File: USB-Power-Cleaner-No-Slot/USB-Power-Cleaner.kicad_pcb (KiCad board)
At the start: 2 copper layers, 43.7 x 17.8 mm, 7 parts, among them J1 USB3_A, J2 USB3_A

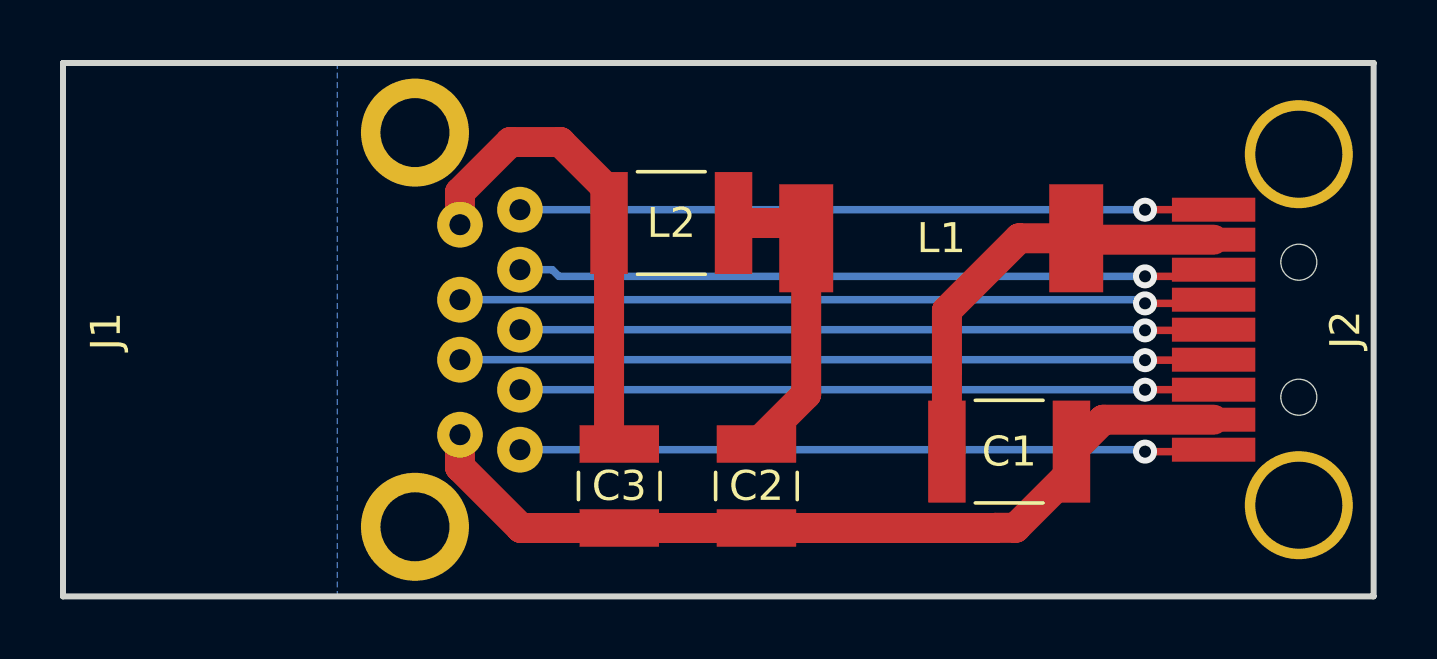
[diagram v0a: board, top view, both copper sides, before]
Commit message: Changed stuff to work better on oshpark board constraints
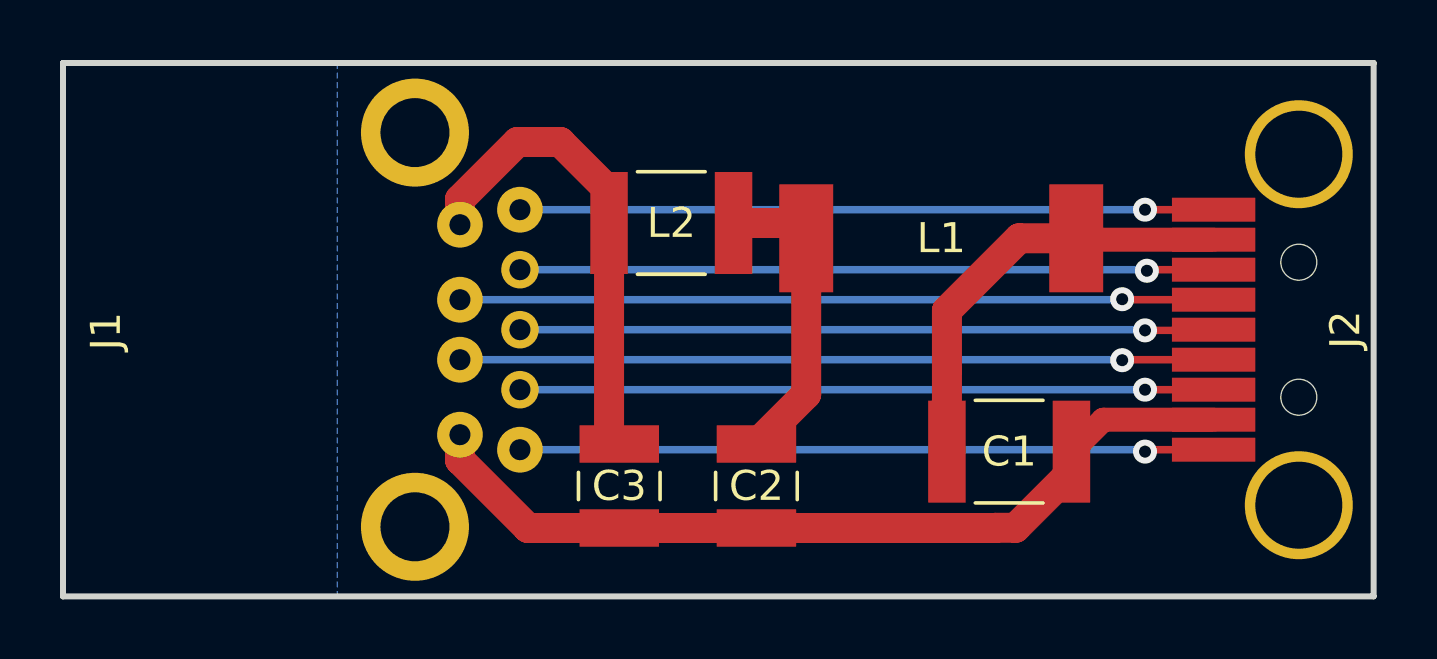
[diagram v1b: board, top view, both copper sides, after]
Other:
- net class Default: clearance 0.1 -> 0.2
- net class Power: clearance 0.1 -> 0.2
- rule trace_clearance: 0.1 -> 0.2
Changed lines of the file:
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@@
     (thickness 1.6)
     (drawings 5)
-    (tracks 62)
+    (tracks 61)
     (zones 0)
     (modules 7)
@@
   (setup
     (last_trace_width 0.25)
-    (trace_clearance 0.1)
+    (trace_clearance 0.2)
     (zone_clearance 0.25)
     (zone_45_only no)
@@
     (mod_text_size 1 1)
     (mod_text_width 0.15)
-    (pad_size 1.524 1.524)
-    (pad_drill 0.762)
+    (pad_size 1.25 1.25)
+    (pad_drill 0.7)
     (pad_to_mask_clearance 0.1)
     (aux_axis_origin 0 0)
@@
   (net 12 "Net-(J1-Pad10)")
   (net_class Default "This is the default net class."
-    (clearance 0.1)
+    (clearance 0.2)
     (trace_width 0.25)
     (via_dia 0.8)
@@
   )
   (net_class Power ""
-    (clearance 0.1)
+    (clearance 0.2)
     (trace_width 1)
     (via_dia 0.8)
@@
     (fp_line (start -7.95 8.35) (end 7.95 8.35) (layer F.CrtYd) (width 0.05))
     (fp_line (start -7.95 8.35) (end -7.95 -8.35) (layer F.CrtYd) (width 0.05))
-    (pad 7 thru_hole circle (at 0 -6.85 270) (size 1.524 1.524) (drill 0.7) (layers *.Cu *.Mask)
+    (pad 7 thru_hole circle (at 0 -6.85 270) (size 1.25 1.25) (drill 0.7) (layers *.Cu *.Mask)
       (net 5 "Net-(J1-Pad7)"))
-    (pad 8 thru_hole circle (at -2 -6.85 270) (size 1.524 1.524) (drill 0.7) (layers *.Cu *.Mask)
+    (pad 8 thru_hole circle (at -2 -6.85 270) (size 1.25 1.25) (drill 0.7) (layers *.Cu *.Mask)
       (net 6 "Net-(J1-Pad8)"))
     (pad 9 thru_hole circle (at -4 -6.85 270) (size 1.524 1.524) (drill 0.7) (layers *.Cu *.Mask)
       (net 7 "Net-(J1-Pad9)"))
-    (pad 6 thru_hole circle (at 2 -6.85 270) (size 1.524 1.524) (drill 0.7) (layers *.Cu *.Mask)
+    (pad 6 thru_hole circle (at 2 -6.85 270) (size 1.25 1.25) (drill 0.7) (layers *.Cu *.Mask)
       (net 8 "Net-(J1-Pad6)"))
     (pad 5 thru_hole circle (at 4 -6.85 270) (size 1.524 1.524) (drill 0.7) (layers *.Cu *.Mask)
@@
   (gr_line (start 157.226 78.74) (end 200.914 78.74) (layer Edge.Cuts) (width 0.2))
   (segment (start 186.69 91.635) (end 186.69 92.71) (width 1) (layer F.Cu) (net 1))
-  (segment (start 191.048 84.63) (end 195.58 84.63) (width 1) (layer F.Cu) (net 1))
+  (segment (start 191.048 84.63) (end 195.58 84.63) (width 0.8) (layer F.Cu) (net 1))
   (segment (start 191 84.582) (end 191.048 84.63) (width 1) (layer F.Cu) (net 1))
   (segment (start 186.69 88.994) (end 186.69 91.694) (width 1) (layer F.Cu) (net 1))
@@
   (segment (start 189.1 84.582) (end 186.69 86.992) (width 1) (layer F.Cu) (net 1))
   (segment (start 191 84.582) (end 189.1 84.582) (width 1) (layer F.Cu) (net 1))
-  (segment (start 173.443 94.24) (end 175.768 94.24) (width 1) (layer F.Cu) (net 2))
-  (segment (start 172.49037 94.24) (end 173.443 94.24) (width 1) (layer F.Cu) (net 2))
-  (segment (start 170.458 92.20763) (end 172.49037 94.24) (width 1) (layer F.Cu) (net 2))
-  (segment (start 170.458 91.13) (end 170.458 92.20763) (width 1) (layer F.Cu) (net 2))
   (segment (start 175.768 94.24) (end 180.34 94.24) (width 1) (layer F.Cu) (net 2))
-  (segment (start 191.904 90.63) (end 190.84 91.694) (width 1) (layer F.Cu) (net 2))
-  (segment (start 195.58 90.63) (end 191.904 90.63) (width 1) (layer F.Cu) (net 2))
+  (segment (start 191.904 90.63) (end 190.84 91.694) (width 0.8) (layer F.Cu) (net 2))
+  (segment (start 195.58 90.63) (end 191.904 90.63) (width 0.8) (layer F.Cu) (net 2))
   (segment (start 190.84 92.37) (end 190.84 91.694) (width 1) (layer F.Cu) (net 2))
   (segment (start 188.976 94.234) (end 190.84 92.37) (width 1) (layer F.Cu) (net 2))
@@
   (segment (start 188.294 94.24) (end 188.3 94.234) (width 1) (layer F.Cu) (net 2))
   (segment (start 180.34 94.24) (end 188.294 94.24) (width 1) (layer F.Cu) (net 2))
+  (segment (start 173.443 94.24) (end 175.768 94.24) (width 1) (layer F.Cu) (net 2))
+  (segment (start 172.726 94.24) (end 173.443 94.24) (width 1) (layer F.Cu) (net 2))
+  (segment (start 170.458 91.972) (end 172.726 94.24) (width 1) (layer F.Cu) (net 2))
+  (segment (start 170.458 91.13) (end 170.458 91.972) (width 1) (layer F.Cu) (net 2))
   (segment (start 181.492 84.074) (end 182 84.582) (width 1) (layer F.Cu) (net 3))
   (segment (start 179.578 84.074) (end 181.492 84.074) (width 1) (layer F.Cu) (net 3))
   (segment (start 182 89.78) (end 180.34 91.44) (width 1) (layer F.Cu) (net 3))
   (segment (start 182 84.582) (end 182 89.78) (width 1) (layer F.Cu) (net 3))
-  (segment (start 175.428 82.999) (end 175.428 84.074) (width 1) (layer F.Cu) (net 4))
-  (segment (start 173.803 81.374) (end 175.428 82.999) (width 1) (layer F.Cu) (net 4))
-  (segment (start 172.13637 81.374) (end 173.803 81.374) (width 1) (layer F.Cu) (net 4))
-  (segment (start 170.458 83.05237) (end 172.13637 81.374) (width 1) (layer F.Cu) (net 4))
-  (segment (start 170.458 84.13) (end 170.458 83.05237) (width 1) (layer F.Cu) (net 4))
   (segment (start 175.428 91.1) (end 175.768 91.44) (width 1) (layer F.Cu) (net 4))
   (segment (start 175.428 84.074) (end 175.428 91.1) (width 1) (layer F.Cu) (net 4))
+  (segment (start 175.428 82.999) (end 175.428 84.074) (width 1) (layer F.Cu) (net 4))
+  (segment (start 170.458 83.288) (end 172.372 81.374) (width 1) (layer F.Cu) (net 4))
+  (segment (start 173.803 81.374) (end 175.428 82.999) (width 1) (layer F.Cu) (net 4))
+  (segment (start 172.372 81.374) (end 173.803 81.374) (width 1) (layer F.Cu) (net 4))
+  (segment (start 170.458 84.13) (end 170.458 83.288) (width 1) (layer F.Cu) (net 4))
   (via (at 193.294 87.652006) (size 0.8) (drill 0.4) (layers F.Cu B.Cu) (net 5))
   (segment (start 193.271994 87.63) (end 193.294 87.652006) (width 0.25) (layer B.Cu) (net 5))
@@
   (segment (start 195.557994 87.652006) (end 195.58 87.63) (width 0.25) (layer F.Cu) (net 5))
   (segment (start 193.294 87.652006) (end 195.557994 87.652006) (width 0.25) (layer F.Cu) (net 5))
-  (segment (start 173.53563 85.63) (end 173.75763 85.852) (width 0.25) (layer B.Cu) (net 6))
-  (segment (start 172.458 85.63) (end 173.53563 85.63) (width 0.25) (layer B.Cu) (net 6))
-  (via (at 193.294 85.852) (size 0.8) (drill 0.4) (layers F.Cu B.Cu) (net 6))
-  (segment (start 173.75763 85.852) (end 193.294 85.852) (width 0.25) (layer B.Cu) (net 6))
-  (segment (start 195.358 85.852) (end 195.58 85.63) (width 0.25) (layer F.Cu) (net 6))
-  (segment (start 193.294 85.852) (end 195.358 85.852) (width 0.25) (layer F.Cu) (net 6))
+  (segment (start 172.458 85.63) (end 193.320926 85.63) (width 0.25) (layer B.Cu) (net 6))
+  (segment (start 195.58 85.63) (end 193.391536 85.63) (width 0.25) (layer F.Cu) (net 6))
+  (segment (start 193.391536 85.63) (end 193.356231 85.665305) (width 0.25) (layer F.Cu) (net 6))
+  (segment (start 193.320926 85.63) (end 193.356231 85.665305) (width 0.25) (layer B.Cu) (net 6))
+  (via (at 193.356231 85.665305) (size 0.8) (drill 0.4) (layers F.Cu B.Cu) (net 6))
   (via (at 193.294 83.63) (size 0.8) (drill 0.4) (layers F.Cu B.Cu) (net 7))
   (segment (start 172.458 83.63) (end 193.294 83.63) (width 0.25) (layer B.Cu) (net 7))
@@
   (segment (start 172.458 89.63) (end 193.294 89.63) (width 0.25) (layer B.Cu) (net 8))
   (segment (start 193.294 89.63) (end 195.58 89.63) (width 0.25) (layer F.Cu) (net 8))
-  (via (at 193.294 91.694) (size 0.8) (drill 0.4) (layers F.Cu B.Cu) (net 9))
-  (segment (start 193.23 91.63) (end 193.294 91.694) (width 0.25) (layer B.Cu) (net 9))
-  (segment (start 172.458 91.63) (end 193.23 91.63) (width 0.25) (layer B.Cu) (net 9))
-  (segment (start 195.516 91.694) (end 195.58 91.63) (width 0.25) (layer F.Cu) (net 9))
-  (segment (start 193.294 91.694) (end 195.516 91.694) (width 0.25) (layer F.Cu) (net 9))
-  (via (at 193.294 86.752003) (size 0.8) (drill 0.4) (layers F.Cu B.Cu) (net 10))
-  (segment (start 193.171997 86.63) (end 193.294 86.752003) (width 0.25) (layer B.Cu) (net 10))
-  (segment (start 170.458 86.63) (end 193.171997 86.63) (width 0.25) (layer B.Cu) (net 10))
-  (segment (start 195.457997 86.752003) (end 195.58 86.63) (width 0.25) (layer F.Cu) (net 10))
-  (segment (start 193.294 86.752003) (end 195.457997 86.752003) (width 0.25) (layer F.Cu) (net 10))
-  (via (at 193.294 88.646) (size 0.8) (drill 0.4) (layers F.Cu B.Cu) (net 11))
-  (segment (start 193.278 88.63) (end 193.294 88.646) (width 0.25) (layer B.Cu) (net 11))
-  (segment (start 170.458 88.63) (end 193.278 88.63) (width 0.25) (layer B.Cu) (net 11))
-  (segment (start 195.564 88.646) (end 195.58 88.63) (width 0.25) (layer F.Cu) (net 11))
-  (segment (start 193.294 88.646) (end 195.564 88.646) (width 0.25) (layer F.Cu) (net 11))
+  (via (at 193.294006 91.694) (size 0.8) (drill 0.4) (layers F.Cu B.Cu) (net 9))
+  (segment (start 193.230006 91.63) (end 193.294006 91.694) (width 0.25) (layer B.Cu) (net 9))
+  (segment (start 172.458 91.63) (end 193.230006 91.63) (width 0.25) (layer B.Cu) (net 9))
+  (segment (start 195.58 91.63) (end 193.358006 91.63) (width 0.25) (layer F.Cu) (net 9))
+  (segment (start 193.358006 91.63) (end 193.294006 91.694) (width 0.25) (layer F.Cu) (net 9))
+  (segment (start 192.516 86.63) (end 192.532 86.614) (width 0.25) (layer B.Cu) (net 10))
+  (via (at 192.532 86.614) (size 0.8) (drill 0.4) (layers F.Cu B.Cu) (net 10))
+  (segment (start 170.458 86.63) (end 192.516 86.63) (width 0.25) (layer B.Cu) (net 10))
+  (segment (start 195.58 86.63) (end 192.548 86.63) (width 0.25) (layer F.Cu) (net 10))
+  (segment (start 192.548 86.63) (end 192.532 86.614) (width 0.25) (layer F.Cu) (net 10))
+  (segment (start 192.548 88.63) (end 192.532 88.646) (width 0.25) (layer F.Cu) (net 11))
+  (segment (start 192.516 88.63) (end 192.532 88.646) (width 0.25) (layer B.Cu) (net 11))
+  (via (at 192.532 88.646) (size 0.8) (drill 0.4) (layers F.Cu B.Cu) (net 11))
+  (segment (start 195.58 88.63) (end 192.548 88.63) (width 0.25) (layer F.Cu) (net 11))
+  (segment (start 170.458 88.63) (end 192.516 88.63) (width 0.25) (layer B.Cu) (net 11))
   (zone (net 12) (net_name "Net-(J1-Pad10)") (layer B.Cu) (hatch edge 0.508)
     (connect_pads (clearance 0.25))
